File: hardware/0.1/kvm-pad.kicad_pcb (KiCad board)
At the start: 2 copper layers, 76.2 x 64.1 mm, 93 parts, among them J1 USB_C_Receptacle_USB2.0, J2 USB_C_Receptacle_USB2.0, J3 AVR-ISP-6, J4 USB_A, J5 USB_A, J6 USB_A, K1 KEYSW, K2 KEYSW, K3 KEYSW, K4 KEYSW, K5 KEYSW, K6 KEYSW, K7 KEYSW, K8 KEYSW, U1 USBLC6-2SC6, U2 ATMEGA32U4, U3 USBLC6-2SC6, U4 TPS211x, U5 TS3USB221E, U6 CY7C65632-28LTXCT, Y1 16MHz, Y2 12MHz

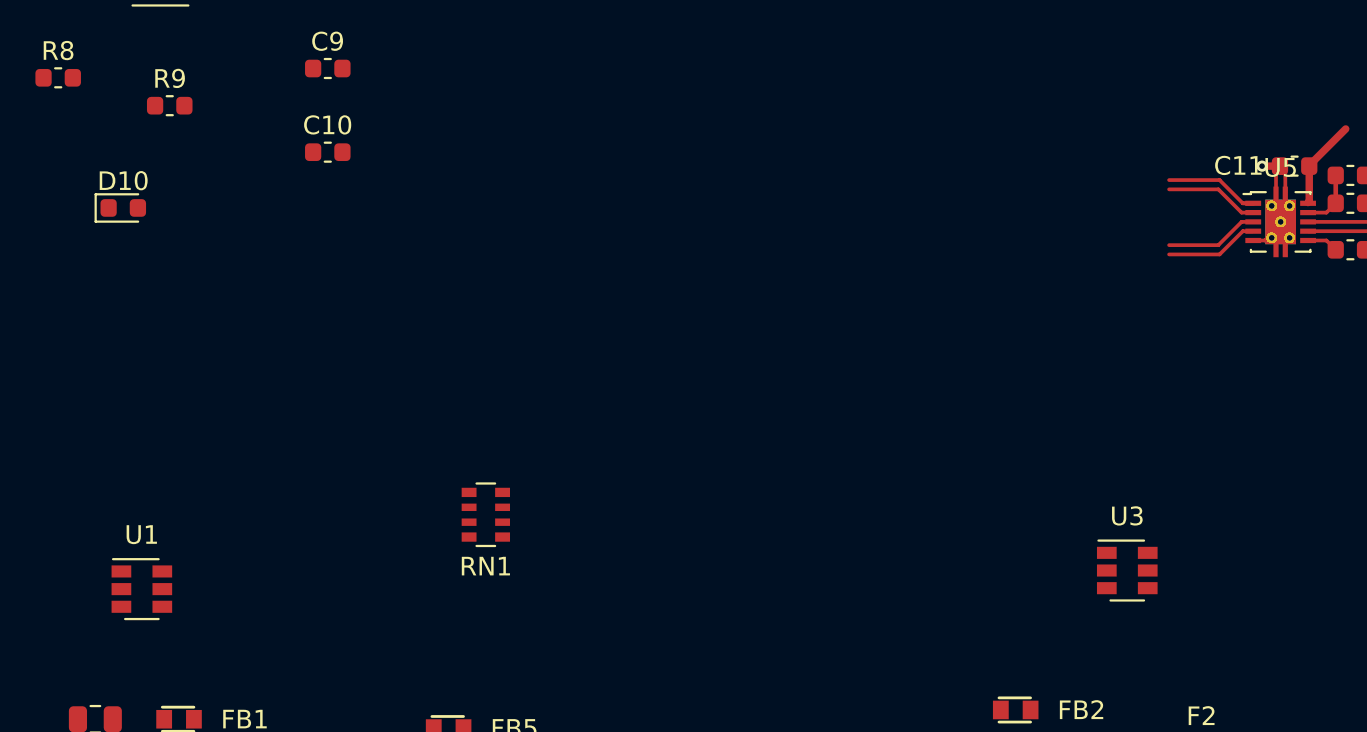
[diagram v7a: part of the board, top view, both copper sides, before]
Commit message: [sch][pcb] Swap USBLC6 IOs for easing PCB routing
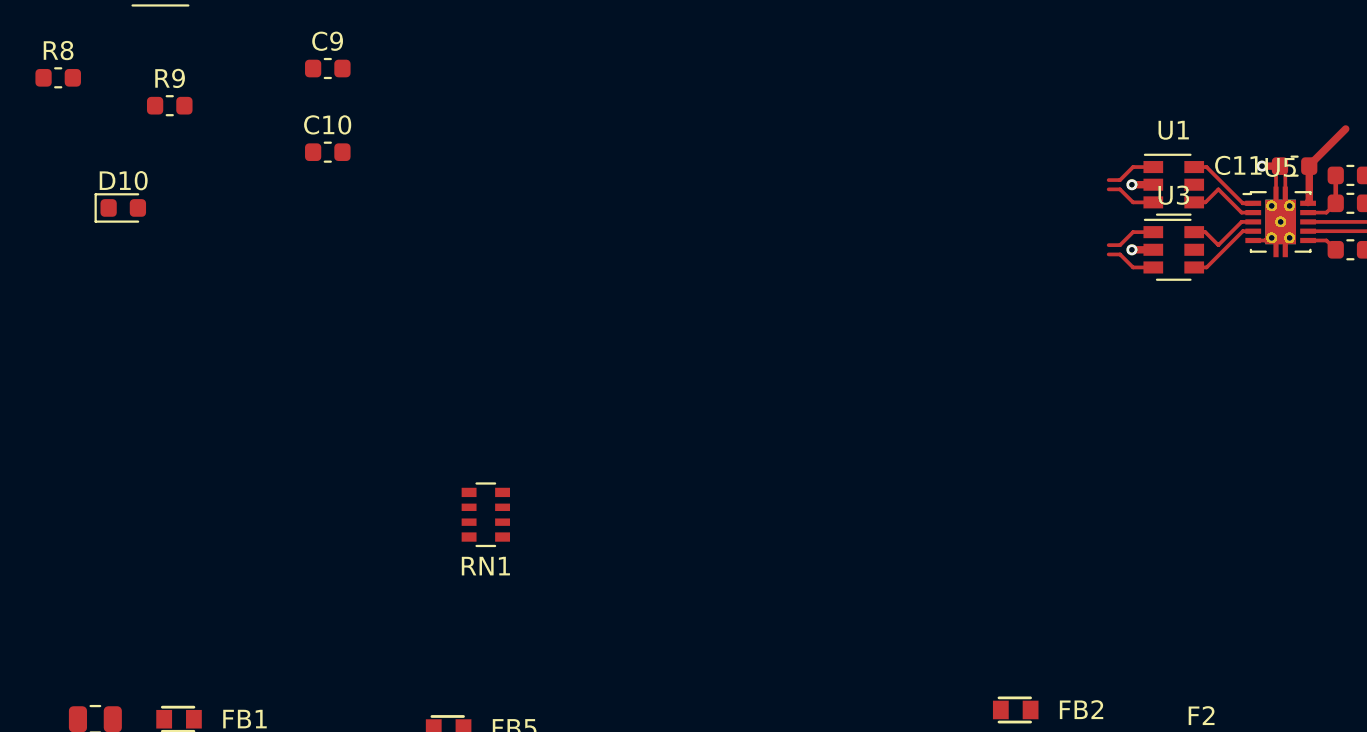
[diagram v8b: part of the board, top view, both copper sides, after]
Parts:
- moved U1 59.6 mm to (74.0, -33.8)
- moved U3 17.4 mm to (74.0, -30.2)
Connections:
- U1 pad 1: /1_D- -> /1_D+
- U1 pad 3: /1_D+ -> /1_D-
- U1 pad 4: /USB_1_D+ -> /USB_1_D-
- U1 pad 6: /USB_1_D- -> /USB_1_D+
- U3 pad 1: /2_D- -> /2_D+
- U3 pad 3: /2_D+ -> /2_D-
- U3 pad 4: /USB_2_D+ -> /USB_2_D-
- U3 pad 6: /USB_2_D- -> /USB_2_D+
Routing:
- net /1_D-: track 0.00 -> 2.69 mm
- net /1_D+: track 0.00 -> 2.69 mm
- net /2_D-: track 0.00 -> 2.69 mm
- net /2_D+: track 0.00 -> 2.69 mm
- net GND: track 29.1 -> 31.4 mm, vias 7 -> 9
- net /USB_2_D-: track 5.04 -> 3.98 mm
- net /USB_2_D+: track 5.04 -> 3.98 mm
- net /USB_1_D-: track 5.04 -> 3.98 mm
- net /USB_1_D+: track 5.44 -> 4.38 mm
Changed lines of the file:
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@@
     (thickness 1.6)
     (drawings 80)
-    (tracks 101)
+    (tracks 118)
     (zones 0)
     (modules 93)
@@
   )
   (setup
-    (last_trace_width 0.4)
+    (last_trace_width 0.2)
     (user_trace_width 0.2)
     (user_trace_width 0.3)
@@
   )
   (module Package_TO_SOT_SMD:SOT-23-6 (layer F.Cu)
-    (at 71.5 -13)
+    (at 74 -30.25)
     (descr "6-pin SOT-23 package")
     (tags SOT-23-6)
@@
       (net 13 /USB_VBUS_2))
     (pad 6 smd rect (at 1.1 -0.95) (size 1.06 0.65) (layers F.Cu F.Paste F.Mask)
-      (net 41 /USB_2_D-))
-    (pad 4 smd rect (at 1.1 0.95) (size 1.06 0.65) (layers F.Cu F.Paste F.Mask)
       (net 42 /USB_2_D+))
+    (pad 4 smd rect (at 1.1 0.95) (size 1.06 0.65) (layers F.Cu F.Paste F.Mask)
+      (net 41 /USB_2_D-))
     (pad 3 smd rect (at -1.1 0.95) (size 1.06 0.65) (layers F.Cu F.Paste F.Mask)
-      (net 21 /2_D+))
+      (net 23 /2_D-))
     (pad 2 smd rect (at -1.1 0) (size 1.06 0.65) (layers F.Cu F.Paste F.Mask)
       (net 1 GND))
     (pad 1 smd rect (at -1.1 -0.95) (size 1.06 0.65) (layers F.Cu F.Paste F.Mask)
-      (net 23 /2_D-))
+      (net 21 /2_D+))
     (model ${KISYS3DMOD}/Package_TO_SOT_SMD.3dshapes/SOT-23-6.wrl
       (at (xyz 0 0 0))
@@
   )
   (module Package_TO_SOT_SMD:SOT-23-6 (layer F.Cu)
-    (at 18.5 -12)
+    (at 74 -33.75)
     (descr "6-pin SOT-23 package")
     (tags SOT-23-6)
@@
       (net 11 /USB_VBUS_1))
     (pad 6 smd rect (at 1.1 -0.95) (size 1.06 0.65) (layers F.Cu F.Paste F.Mask)
-      (net 39 /USB_1_D-))
-    (pad 4 smd rect (at 1.1 0.95) (size 1.06 0.65) (layers F.Cu F.Paste F.Mask)
       (net 40 /USB_1_D+))
+    (pad 4 smd rect (at 1.1 0.95) (size 1.06 0.65) (layers F.Cu F.Paste F.Mask)
+      (net 39 /USB_1_D-))
     (pad 3 smd rect (at -1.1 0.95) (size 1.06 0.65) (layers F.Cu F.Paste F.Mask)
-      (net 17 /1_D+))
+      (net 19 /1_D-))
     (pad 2 smd rect (at -1.1 0) (size 1.06 0.65) (layers F.Cu F.Paste F.Mask)
       (net 1 GND))
     (pad 1 smd rect (at -1.1 -0.95) (size 1.06 0.65) (layers F.Cu F.Paste F.Mask)
-      (net 19 /1_D-))
+      (net 17 /1_D+))
     (model ${KISYS3DMOD}/Package_TO_SOT_SMD.3dshapes/SOT-23-6.wrl
       (at (xyz 0 0 0))
@@
   (segment (start 119.0375 -43.75) (end 119.0375 -33.25) (width 0.4) (layer F.Cu) (net 1))
   (segment (start 127.612501 59) (end 127.612501 62) (width 0.4) (layer F.Cu) (net 1))
+  (via (at 71.75 -30.25) (size 0.6) (drill 0.3) (layers F.Cu B.Cu) (net 1))
+  (segment (start 72.9 -30.25) (end 71.75 -30.25) (width 0.4) (layer F.Cu) (net 1))
+  (via (at 71.75 -33.75) (size 0.6) (drill 0.3) (layers F.Cu B.Cu) (net 1))
+  (segment (start 72.9 -33.75) (end 71.75 -33.75) (width 0.4) (layer F.Cu) (net 1))
   (segment (start 117.4625 -36.25) (end 117.4625 -33.25) (width 0.2) (layer F.Cu) (net 2))
   (segment (start 117.4125 -36.2) (end 117.4625 -36.25) (width 0.4) (layer F.Cu) (net 2))
@@
   (segment (start 117 -17.434302) (end 115.600001 -16.034303) (width 0.2) (layer F.Cu) (net 7))
   (segment (start 126.037501 59) (end 126.037501 62) (width 0.4) (layer F.Cu) (net 8))
+  (segment (start 72.9 -34.7) (end 71.811998 -34.7) (width 0.2) (layer F.Cu) (net 17))
+  (segment (start 71.811998 -34.7) (end 71.111998 -34) (width 0.2) (layer F.Cu) (net 17))
+  (segment (start 71.111998 -34) (end 70.5 -34) (width 0.2) (layer F.Cu) (net 17))
+  (segment (start 72.9 -32.8) (end 71.811998 -32.8) (width 0.2) (layer F.Cu) (net 19))
+  (segment (start 71.811998 -32.8) (end 71.111998 -33.5) (width 0.2) (layer F.Cu) (net 19))
+  (segment (start 71.111998 -33.5) (end 70.5 -33.5) (width 0.2) (layer F.Cu) (net 19))
+  (segment (start 72.9 -31.2) (end 71.811998 -31.2) (width 0.2) (layer F.Cu) (net 21))
+  (segment (start 71.811998 -31.2) (end 71.111998 -30.5) (width 0.2) (layer F.Cu) (net 21))
+  (segment (start 71.111998 -30.5) (end 70.5 -30.5) (width 0.2) (layer F.Cu) (net 21))
+  (segment (start 72.9 -29.3) (end 71.811998 -29.3) (width 0.2) (layer F.Cu) (net 23))
+  (segment (start 71.811998 -29.3) (end 71.111998 -30) (width 0.2) (layer F.Cu) (net 23))
+  (segment (start 71.111998 -30) (end 70.5 -30) (width 0.2) (layer F.Cu) (net 23))
   (segment (start 114.55 -19) (end 114.20303 -19) (width 0.2) (layer F.Cu) (net 25))
   (segment (start 114.20303 -19) (end 112.70303 -17.5) (width 0.2) (layer F.Cu) (net 25))
@@
   (segment (start 77.65 -32.25) (end 76.4 -33.5) (width 0.2) (layer F.Cu) (net 39))
   (segment (start 78.275 -32.25) (end 77.65 -32.25) (width 0.2) (layer F.Cu) (net 39))
-  (segment (start 76.4 -33.5) (end 73.75 -33.5) (width 0.2) (layer F.Cu) (net 39))
+  (segment (start 75.7 -32.8) (end 75.1 -32.8) (width 0.2) (layer F.Cu) (net 39))
+  (segment (start 76.4 -33.5) (end 75.7 -32.8) (width 0.2) (layer F.Cu) (net 39))
   (segment (start 78.275 -32.75) (end 77.875 -32.75) (width 0.25) (layer F.Cu) (net 40))
-  (segment (start 78.275 -32.75) (end 77.75 -32.75) (width 0.2) (layer F.Cu) (net 40))
-  (segment (start 77.715698 -32.75) (end 76.465698 -34) (width 0.2) (layer F.Cu) (net 40))
-  (segment (start 77.75 -32.75) (end 77.715698 -32.75) (width 0.2) (layer F.Cu) (net 40))
-  (segment (start 76.465698 -34) (end 73.75 -34) (width 0.2) (layer F.Cu) (net 40))
-  (segment (start 77.715698 -31.25) (end 76.465698 -30) (width 0.2) (layer F.Cu) (net 41))
+  (segment (start 75.765698 -34.7) (end 75.1 -34.7) (width 0.2) (layer F.Cu) (net 40))
+  (segment (start 77.715698 -32.75) (end 75.765698 -34.7) (width 0.2) (layer F.Cu) (net 40))
+  (segment (start 78.275 -32.75) (end 77.715698 -32.75) (width 0.2) (layer F.Cu) (net 40))
+  (segment (start 77.715698 -31.25) (end 75.765698 -29.3) (width 0.2) (layer F.Cu) (net 41))
+  (segment (start 75.765698 -29.3) (end 75.1 -29.3) (width 0.2) (layer F.Cu) (net 41))
   (segment (start 78.275 -31.25) (end 77.715698 -31.25) (width 0.2) (layer F.Cu) (net 41))
-  (segment (start 76.465698 -30) (end 73.75 -30) (width 0.2) (layer F.Cu) (net 41))
   (segment (start 77.65 -31.75) (end 76.4 -30.5) (width 0.2) (layer F.Cu) (net 42))
   (segment (start 78.275 -31.75) (end 77.65 -31.75) (width 0.2) (layer F.Cu) (net 42))
-  (segment (start 76.4 -30.5) (end 73.75 -30.5) (width 0.2) (layer F.Cu) (net 42))
+  (segment (start 75.7 -31.2) (end 75.1 -31.2) (width 0.2) (layer F.Cu) (net 42))
+  (segment (start 76.4 -30.5) (end 75.7 -31.2) (width 0.2) (layer F.Cu) (net 42))
   (segment (start 81.225 -31.25) (end 88.5 -31.25) (width 0.2) (layer F.Cu) (net 43))
   (segment (start 81.225 -31.75) (end 88.5 -31.75) (width 0.2) (layer F.Cu) (net 44))
